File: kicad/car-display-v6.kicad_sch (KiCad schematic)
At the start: 43 parts, among them J1 AVR-ISP-10, J2 Screw_Terminal_01x03, J3 PicoBlade F 1x7, J4 Socket 1x6 0.1", U1 ATmega328PB-M, U2 MCP25625T-E/ML, U3 3.3V, U4 TPSM365R15FRDNR, U5 TPS3422, Y1 16MHZ

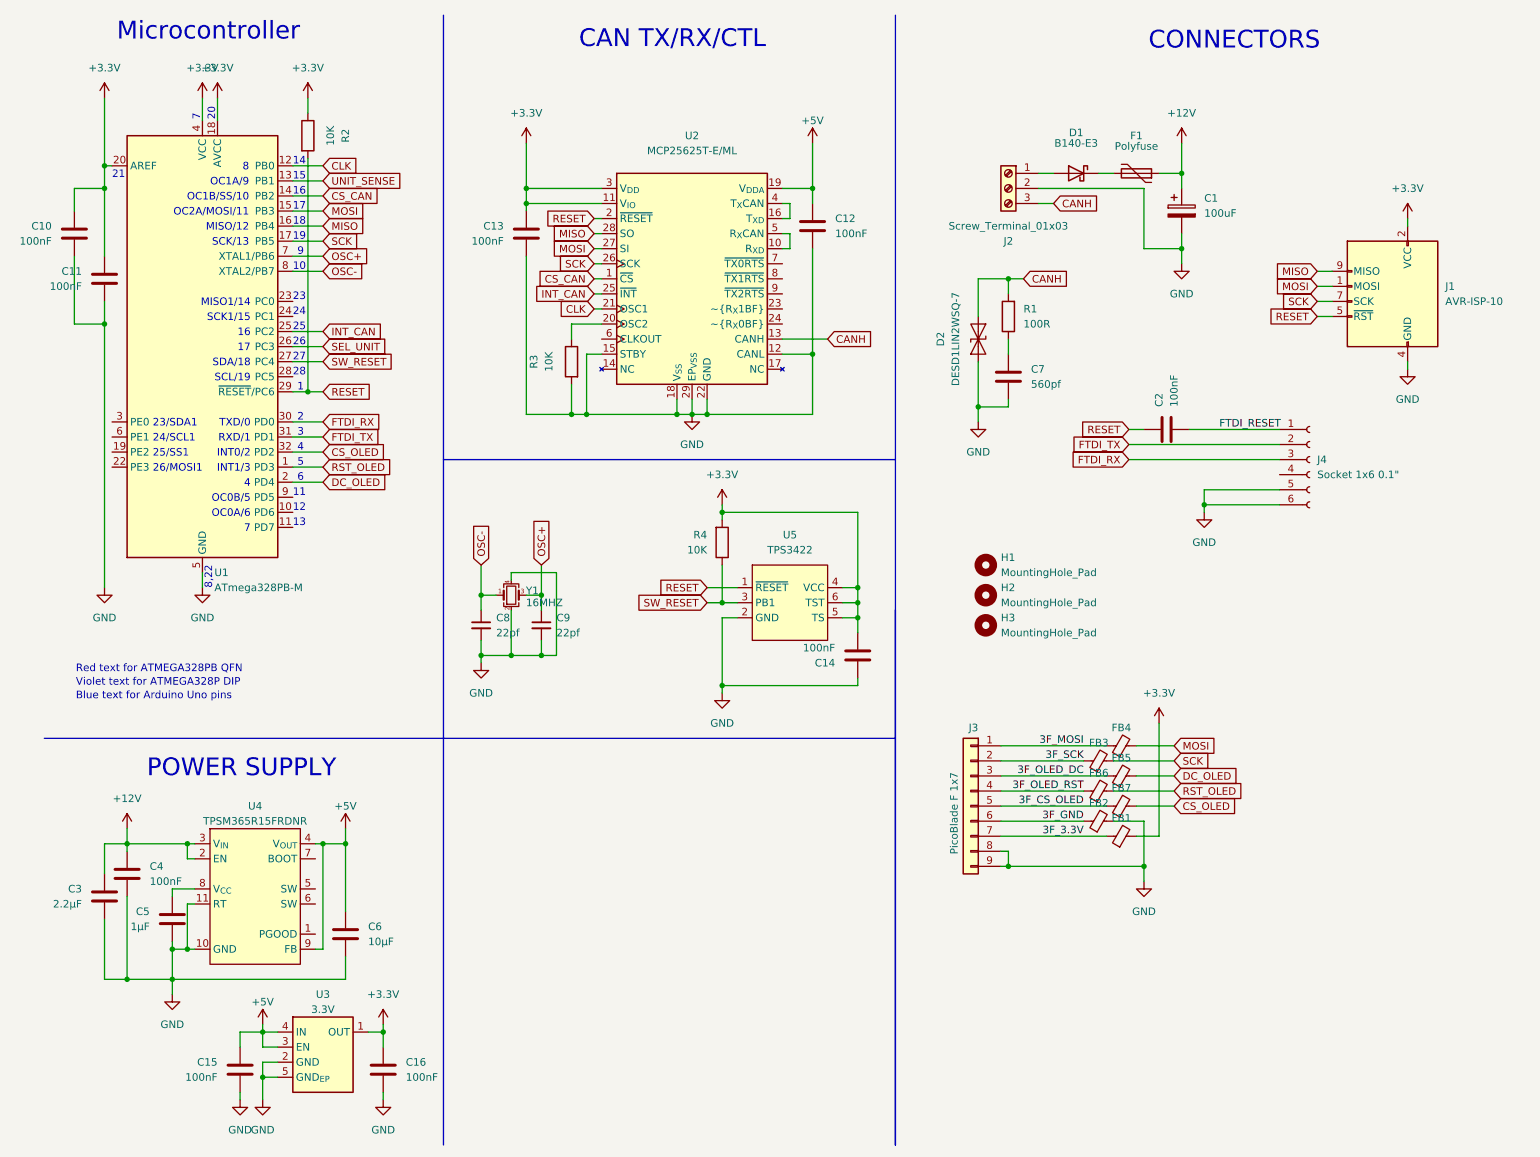
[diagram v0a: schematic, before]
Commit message: Update PCB connectors
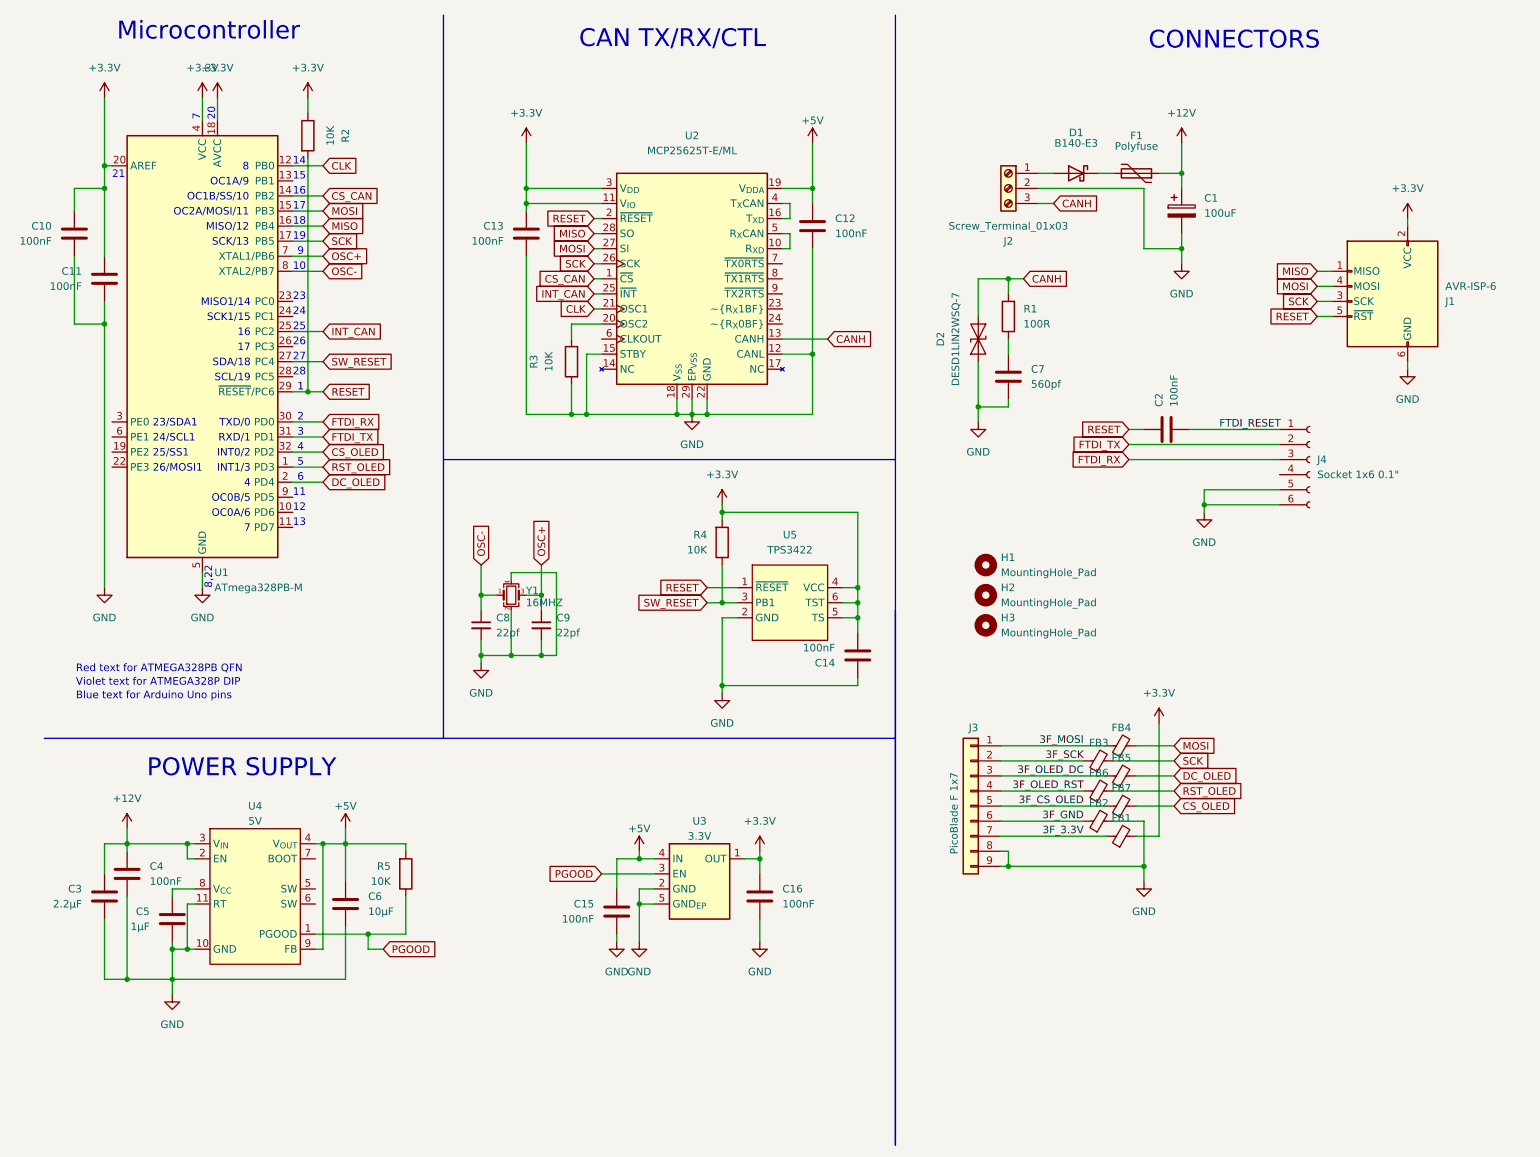
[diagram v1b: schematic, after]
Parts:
- removed J1: AVR-ISP-10, jsdev:PinHeader_SWD_BD120-10-A-0305-0229-L-B, symbol Connector:AVR-ISP-10
- added J1: AVR-ISP-6, jsdev:PinHeader_ISP_POGO, symbol Connector:AVR-ISP-6
- added R5: 10K, Resistor_SMD:R_0402_1005Metric, symbol Device:R
- U4: value TPSM365R15FRDNR -> 5V
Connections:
- net +3.3V: now also J1.2 (VCC)
- net +5V: now also R5.2; no longer U3.3 (EN)
- net GND: now also J1.6 (GND)
- net MISO: now also J1.1 (MISO)
- net MOSI: now also J1.4 (MOSI)
- net RESET: now also J1.5 (~{RST})
- net SCK: now also J1.3 (SCK)
- net PGOOD: now reaches U4.1 (PGOOD)
- net PGOOD: now also U3.3 (EN), R5.1
- net SEL_UNIT: no longer names the net of U1.26 (PC3)
- net UNIT_SENSE: no longer names the net of U1.13 (PB1)
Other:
- moved on the sheet: C15, C16, C6, U3

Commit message: Move some pins around
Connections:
- net CS_CAN: now also U1.11 (PD7); no longer U1.14 (PB2)
- net SW_RESET: now also U1.26 (PC3); no longer U1.27 (PC4)

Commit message: Production cleanup
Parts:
- R5: value 10K -> 100K

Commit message: Production cleanup
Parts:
- R4: value 10K -> 100K
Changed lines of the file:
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@@
 			)
 		)
-		(property "Value" "10K"
+		(property "Value" "100K"
 			(at 124.46 102.8699 0)
 			(effects
